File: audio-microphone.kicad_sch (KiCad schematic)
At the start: 9 parts, among them J1 JST_SUR_1x5_BM05B-SURS-TB-LF-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

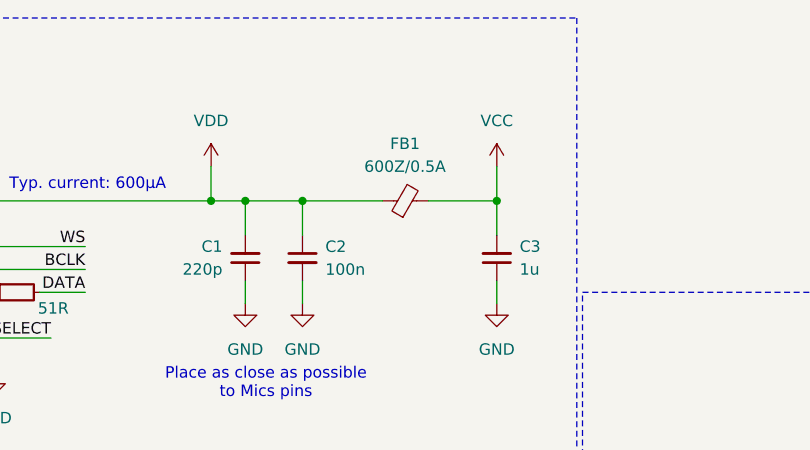
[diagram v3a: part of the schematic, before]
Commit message: [#71550] Change FB1 to 0402 size one BLM15AG601SN1D
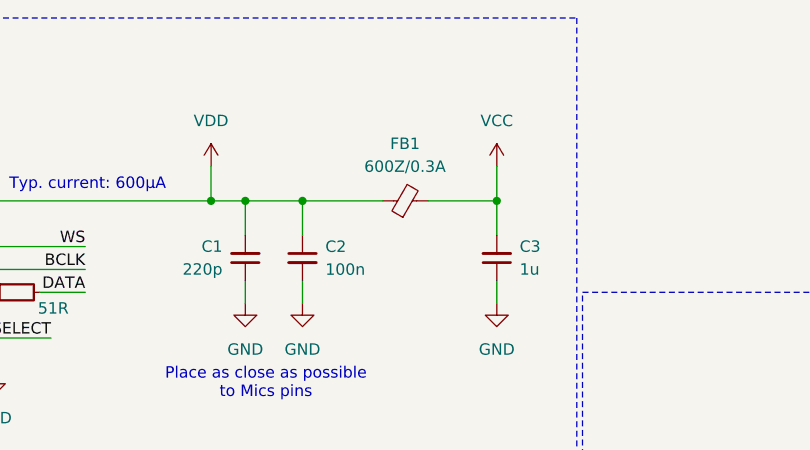
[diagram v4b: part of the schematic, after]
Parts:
- removed FB1: FB_600Z_0.5A_Murata-BLM18AG_0603, antmicro-footprints:FB_0603_1608Metric, symbol antmicroFerriteBeadsandChips:FB_600Z_0.5A_Murata-BLM18AG_0603
- added FB1: FB_600Z_0.3A_Murata-BLM15AG_0402, antmicro-footprints:FB_0402_1005Metric, symbol antmicroFerriteBeadsandChips:FB_600Z_0.3A_Murata-BLM15AG_0402
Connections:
- net VCC: now also FB1.2
- net VDD: now also FB1.1
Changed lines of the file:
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@@
 	(label "DATA"
 		(at 182.88 100.33 0)
-		(fields_autoplaced yes)
 		(effects
 			(font
@@
 	(label "DATA"
 		(at 99.06 69.85 180)
-		(fields_autoplaced yes)
 		(effects
 			(font
@@
 	(label "SELECT"
 		(at 95.25 74.93 180)
-		(fields_autoplaced yes)
 		(effects
 			(font
@@
 	(label "WS"
 		(at 182.88 97.79 0)
-		(fields_autoplaced yes)
 		(effects
 			(font
@@
 	(label "SELECT"
 		(at 97.79 123.19 0)
-		(fields_autoplaced yes)
 		(effects
 			(font
@@
 	(label "BCLK"
 		(at 99.06 67.31 180)
-		(fields_autoplaced yes)
 		(effects
 			(font
@@
 	(label "WS"
 		(at 99.06 64.77 180)
-		(fields_autoplaced yes)
 		(effects
 			(font
@@
 	(label "BCLK"
 		(at 182.88 95.25 0)
-		(fields_autoplaced yes)
 		(effects
 			(font
@@
 	)
 	(symbol
-		(lib_id "antmicroFerriteBeadsandChips:FB_600Z_0.5A_Murata-BLM18AG_0603")
-		(at 132.08 59.69 0)
-		(unit 1)
-		(exclude_from_sim no)
-		(in_bom yes)
-		(on_board yes)
-		(dnp no)
-		(fields_autoplaced yes)
-		(property "Reference" "FB1"
-			(at 134.5819 53.34 0)
-			(effects
-				(font
-					(size 1.27 1.27)
-					(thickness 0.15)
-				)
-			)
-		)
-		(property "Value" "FB_600Z_0.5A_Murata-BLM18AG_0603"
-			(at 147.32 62.23 0)
-			(effects
-				(font
-					(size 1.27 1.27)
-					(thickness 0.15)
-				)
-				(justify left bottom)
-				(hide yes)
-			)
-		)
-		(property "Footprint" "antmicro-footprints:FB_0603_1608Metric"
-			(at 147.32 67.31 0)
-			(effects
-				(font
-					(size 1.27 1.27)
-					(thickness 0.15)
-				)
-				(justify left bottom)
-				(hide yes)
-			)
-		)
-		(property "Datasheet" "https://www.murata.com/en-us/products/productdata/8796738650142/ENFA0003.pdf"
-			(at 147.32 69.85 0)
-			(effects
-				(font
-					(size 1.27 1.27)
-					(thickness 0.15)
-				)
-				(justify left bottom)
-				(hide yes)
-			)
-		)
-		(property "Description" "Ferrite Bead, 0603 [1608 Metric], 600 ohm, 500 mA, BLM18A, 0.38 ohm, ± 25%, General use"
-			(at 132.08 59.69 0)
-			(effects
-				(font
-					(size 1.27 1.27)
-				)
-				(hide yes)
-			)
-		)
-		(property "Val" "600Z/0.5A"
-			(at 134.5819 55.88 0)
-			(effects
-				(font
-					(size 1.27 1.27)
-				)
-			)
-		)
-		(property "MPN" "BLM18AG601SN1D"
-			(at 147.32 72.39 0)
-			(effects
-				(font
-					(size 1.27 1.27)
-					(thickness 0.15)
-				)
-				(justify left bottom)
-				(hide yes)
-			)
-		)
-		(property "Manufacturer" "Murata"
-			(at 147.32 74.93 0)
-			(effects
-				(font
-					(size 1.27 1.27)
-					(thickness 0.15)
-				)
-				(justify left bottom)
-				(hide yes)
-			)
-		)
-		(property "Current" ""
-			(at 152.4 82.55 0)
-			(effects
-				(font
-					(size 1.27 1.27)
-					(thickness 0.15)
-				)
-				(justify left bottom)
-				(hide yes)
-			)
-		)
-		(property "Author" "Antmicro"
-			(at 147.32 77.47 0)
-			(effects
-				(font
-					(size 1.27 1.27)
-					(thickness 0.15)
-				)
-				(justify left bottom)
-				(hide yes)
-			)
-		)
-		(property "License" "Apache-2.0"
-			(at 147.32 80.01 0)
-			(effects
-				(font
-					(size 1.27 1.27)
-					(thickness 0.15)
-				)
-				(justify left bottom)
-				(hide yes)
-			)
-		)
-		(pin "1"
-		)
-		(pin "2"
-		)
-		(instances
-			(project ""
-				(path "/4a2cf8c5-6ba3-448d-b2e4-bea2166340e3"
-					(reference "FB1")
-					(unit 1)
-				)
-			)
-		)
-	)
-	(symbol
 		(lib_id "antmicropower:VDD")
 		(at 165.1 140.97 0)
@@
 					(unit 1)
 				)
+			)
+		)
+	)
+	(symbol
+		(lib_id "antmicroFerriteBeadsandChips:FB_600Z_0.3A_Murata-BLM15AG_0402")
+		(at 132.08 59.69 0)
+		(unit 1)
+		(exclude_from_sim no)
+		(in_bom yes)
+		(on_board yes)
+		(dnp no)
+		(fields_autoplaced yes)
+		(property "Reference" "FB1"
+			(at 134.5819 53.34 0)
+			(effects
+				(font
+					(size 1.27 1.27)
+					(thickness 0.15)
+				)
+			)
+		)
+		(property "Value" "FB_600Z_0.3A_Murata-BLM15AG_0402"
+			(at 147.32 62.23 0)
+			(effects
+				(font
+					(size 1.27 1.27)
+					(thickness 0.15)
+				)
+				(justify left bottom)
+				(hide yes)
+			)
+		)
+		(property "Footprint" "antmicro-footprints:FB_0402_1005Metric"
+			(at 147.32 67.31 0)
+			(effects
+				(font
+					(size 1.27 1.27)
+					(thickness 0.15)
+				)
+				(justify left bottom)
+				(hide yes)
+			)
+		)
+		(property "Datasheet" "https://www.murata.com/en-us/products/productdata/8796740059166/ENFA0018.pdf"
+			(at 147.32 69.85 0)
+			(effects
+				(font
+					(size 1.27 1.27)
+					(thickness 0.15)
+				)
+				(justify left bottom)
+				(hide yes)
+			)
+		)
+		(property "Description" "Ferrite Bead, 0402 [1005 Metric], 600 ohm, 300 mA, BLM15AG_SN, 0.6 ohm, ± 25%, General use"
+			(at 132.08 59.69 0)
+			(effects
+				(font
+					(size 1.27 1.27)
+				)
+				(hide yes)
+			)
+		)
+		(property "Val" "600Z/0.3A"
+			(at 134.5819 55.88 0)
+			(effects
+				(font
+					(size 1.27 1.27)
+				)
+			)
+		)
+		(property "MPN" "BLM15AG601SN1D"
+			(at 147.32 72.39 0)
+			(effects
+				(font
+					(size 1.27 1.27)
+					(thickness 0.15)
+				)
+				(justify left bottom)
+				(hide yes)
+			)
+		)
+		(property "Manufacturer" "Murata"
+			(at 147.32 74.93 0)
+			(effects
+				(font
+					(size 1.27 1.27)
+					(thickness 0.15)
+				)
+				(justify left bottom)
+				(hide yes)
+			)
+		)
+		(property "Current" ""
+			(at 152.4 82.55 0)
+			(effects
+				(font
+					(size 1.27 1.27)
+					(thickness 0.15)
+				)
+				(justify left bottom)
+				(hide yes)
+			)
+		)
+		(property "Author" "Antmicro"
+			(at 147.32 77.47 0)
+			(effects
+				(font
+					(size 1.27 1.27)
+					(thickness 0.15)
+				)
+				(justify left bottom)
+				(hide yes)
+			)
+		)
+		(property "License" "Apache-2.0"
+			(at 147.32 80.01 0)
+			(effects
+				(font
+					(size 1.27 1.27)
+					(thickness 0.15)
+				)
+				(justify left bottom)
+				(hide yes)
+			)
+		)
+		(pin "2"
+		)
+		(pin "1"
+		)
+		(instances
+			(project ""
+				(path "/4a2cf8c5-6ba3-448d-b2e4-bea2166340e3"
+					(reference "FB1")
+					(unit 1)
+				)

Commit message: [#71550] Remove dash from sch name
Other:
- title: audio-microphone -> Audio Microphone
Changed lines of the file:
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@@
 	(paper "A4")
 	(title_block
-		(title "audio-microphone")
+		(title "Audio Microphone")
 		(date "07.01.2025")
 		(rev "1.0.0")
@@
 	(label "DATA"
 		(at 182.88 100.33 0)
+		(fields_autoplaced yes)
 		(effects
 			(font
@@
 	(label "DATA"
 		(at 99.06 69.85 180)
+		(fields_autoplaced yes)
 		(effects
 			(font
@@
 	(label "SELECT"
 		(at 95.25 74.93 180)
+		(fields_autoplaced yes)
 		(effects
 			(font
@@
 	(label "WS"
 		(at 182.88 97.79 0)
+		(fields_autoplaced yes)
 		(effects
 			(font
@@
 	(label "SELECT"
 		(at 97.79 123.19 0)
+		(fields_autoplaced yes)
 		(effects
 			(font
@@
 	(label "BCLK"
 		(at 99.06 67.31 180)
+		(fields_autoplaced yes)
 		(effects
 			(font
@@
 	(label "WS"
 		(at 99.06 64.77 180)
+		(fields_autoplaced yes)
 		(effects
 			(font
@@
 	(label "BCLK"
 		(at 182.88 95.25 0)
-		(effects
-			(font
+		(fields_autoplaced yes)
+		(effects
+			(font
